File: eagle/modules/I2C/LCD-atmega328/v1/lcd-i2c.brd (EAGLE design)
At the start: 49.5 x 38.1 mm, 19 parts, among them IC2 MEGA8-AI, J1 RJ12RIGHTANGLE-I2C, J4 RJ12RIGHTANGLE-I2C, Q1 BC349

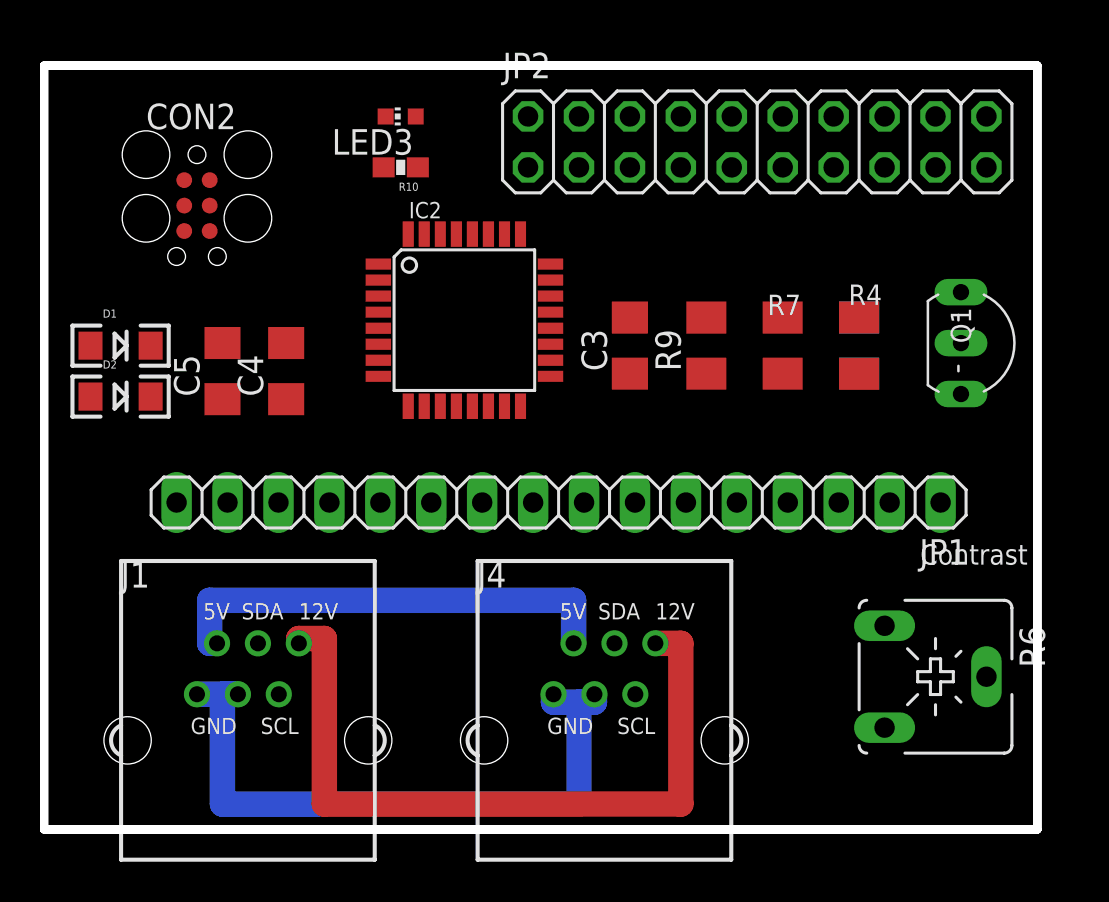
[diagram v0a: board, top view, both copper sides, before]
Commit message: update atmeaga328 i2c
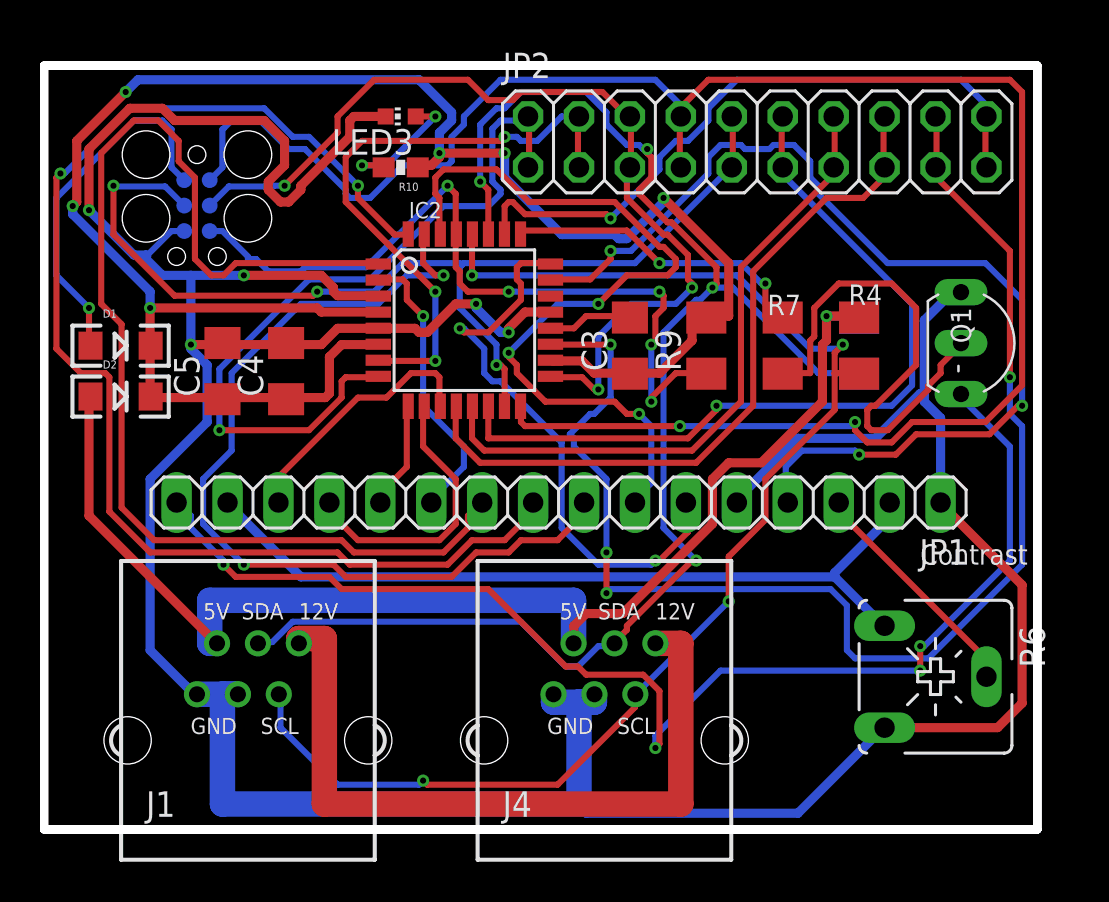
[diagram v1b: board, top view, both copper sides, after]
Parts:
- flipped CON2 to the bottom
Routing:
- net GND: track 34.0 -> 182.2 mm, vias 0 -> 5
- net +5V: track 0.00 -> 97.0 mm, vias 0 -> 6
- net MISO: track 0.00 -> 95.5 mm, vias 0 -> 2
- net SDA: track 0.00 -> 75.3 mm, vias 0 -> 4
- net SCL: track 0.00 -> 68.1 mm, vias 0 -> 4
- net A6: track 0.00 -> 66.8 mm, vias 0 -> 4
- net D2: track 0.00 -> 64.2 mm, vias 0 -> 2
- net N$7: track 0.00 -> 63.3 mm, vias 0 -> 4
- net D3: track 0.00 -> 59.3 mm
- net MOSI: track 0.00 -> 51.9 mm, vias 0 -> 3
- net RS: track 0.00 -> 51.4 mm, vias 0 -> 3
- net SCK: track 0.00 -> 46.3 mm, vias 0 -> 3
- net D1: track 0.00 -> 45.4 mm, vias 0 -> 2
- net 5V_B: track 22.8 -> 64.8 mm, vias 0 -> 1
- net D0: track 0.00 -> 40.6 mm, vias 0 -> 3
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
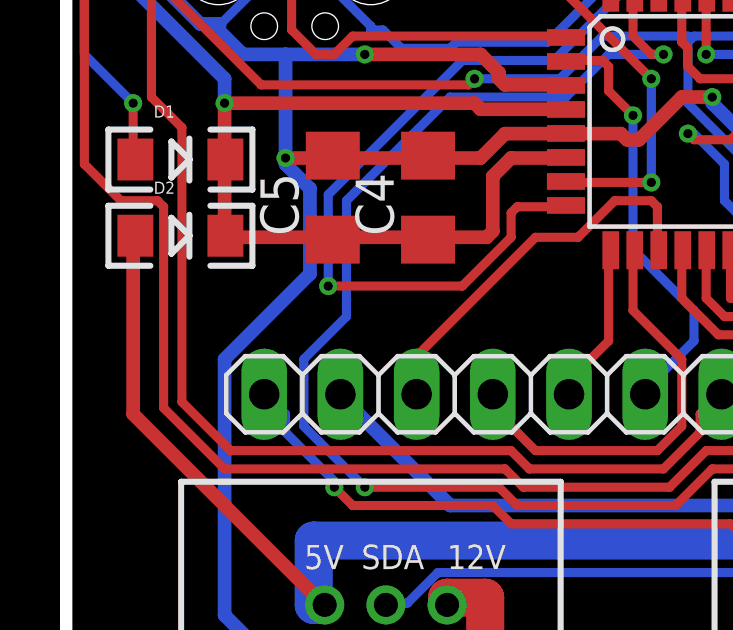
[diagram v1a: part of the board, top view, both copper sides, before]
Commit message: Correct LCD
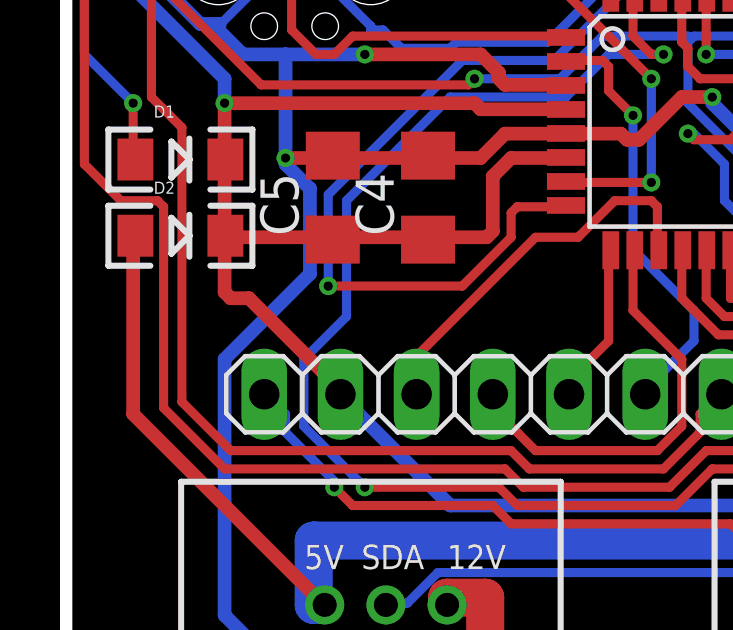
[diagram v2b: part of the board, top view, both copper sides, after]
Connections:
- removed net VCC: JP1.15, JP1.2, R6.A
- net +5V: now also JP1.15, JP1.2, R6.A
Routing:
- net +5V: track 97.0 -> 144.4 mm
- net VCC: track 40.2 -> 0.00 mm
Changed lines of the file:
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@@
 </elements>
 <signals>
-<signal name="VCC" class="1">
-<contactref element="JP1" pad="15"/>
-<contactref element="JP1" pad="2"/>
-<contactref element="R6" pad="A"/>
-<wire x1="12.8016" y1="12.5984" x2="9.144" y2="16.256" width="0.4572" layer="16"/>
-<wire x1="39.4208" y1="12.5984" x2="12.8016" y2="12.5984" width="0.4572" layer="16"/>
-<wire x1="41.8592" y1="10.16" x2="39.4208" y2="12.5984" width="0.4572" layer="16"/>
-<wire x1="9.144" y1="16.256" x2="9.144" y2="16.3068" width="0.4572" layer="16"/>
-<wire x1="41.8592" y1="10.16" x2="41.91" y2="10.16" width="0.4572" layer="16"/>
-<wire x1="42.0624" y1="15.4432" x2="42.0624" y2="16.256" width="0.4572" layer="16"/>
-<wire x1="39.4208" y1="12.8016" x2="42.0624" y2="15.4432" width="0.4572" layer="16"/>
-<wire x1="42.0624" y1="16.256" x2="42.164" y2="16.3068" width="0.4572" layer="16"/>
-<wire x1="39.4208" y1="12.8016" x2="39.4208" y2="12.5984" width="0.4572" layer="16"/>
-</signal>
 <signal name="GND" class="1">
 <contactref element="Q1" pad="E"/>
@@
 <via x="30.8864" y="31.496" extent="1-16" drill="0.3048"/>
 <via x="22.9616" y="33.7312" extent="1-16" drill="0.3048"/>
+<contactref element="JP1" pad="2"/>
+<contactref element="R6" pad="A"/>
+<contactref element="JP1" pad="15"/>
+<wire x1="12.8016" y1="12.5984" x2="9.144" y2="16.256" width="0.4572" layer="16"/>
+<wire x1="39.4208" y1="12.5984" x2="12.8016" y2="12.5984" width="0.4572" layer="16"/>
+<wire x1="41.8592" y1="10.16" x2="39.4208" y2="12.5984" width="0.4572" layer="16"/>
+<wire x1="9.144" y1="16.256" x2="9.144" y2="16.3068" width="0.4572" layer="16"/>
+<wire x1="42.0624" y1="15.4432" x2="42.0624" y2="16.256" width="0.4572" layer="16"/>
+<wire x1="39.4208" y1="12.8016" x2="42.0624" y2="15.4432" width="0.4572" layer="16"/>
+<wire x1="39.4208" y1="12.8016" x2="39.4208" y2="12.5984" width="0.4572" layer="16"/>
+<wire x1="41.8592" y1="10.16" x2="41.91" y2="10.16" width="0.4572" layer="16"/>
+<wire x1="42.0624" y1="16.256" x2="42.164" y2="16.3068" width="0.4572" layer="16"/>
+<wire x1="6.096" y1="19.5072" x2="9.144" y2="16.4592" width="0.4572" layer="1"/>
+<wire x1="5.4864" y1="19.5072" x2="6.096" y2="19.5072" width="0.4572" layer="1"/>
+<wire x1="5.2832" y1="19.7104" x2="5.4864" y2="19.5072" width="0.4572" layer="1"/>
+<wire x1="5.2832" y1="21.5392" x2="5.2832" y2="19.7104" width="0.4572" layer="1"/>
+<wire x1="9.144" y1="16.4592" x2="9.144" y2="16.3068" width="0.4572" layer="1"/>
+<wire x1="5.2832" y1="21.5392" x2="5.31" y2="21.59" width="0.4572" layer="1"/>
 </signal>
 <signal name="SCK">
